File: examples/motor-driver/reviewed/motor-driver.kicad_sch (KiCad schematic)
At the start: 12 parts, among them J1 VM 2.7-10.8V, J2 MOTOR A, J3 MOTOR B, J4 LOGIC, U1 DRV8833PW

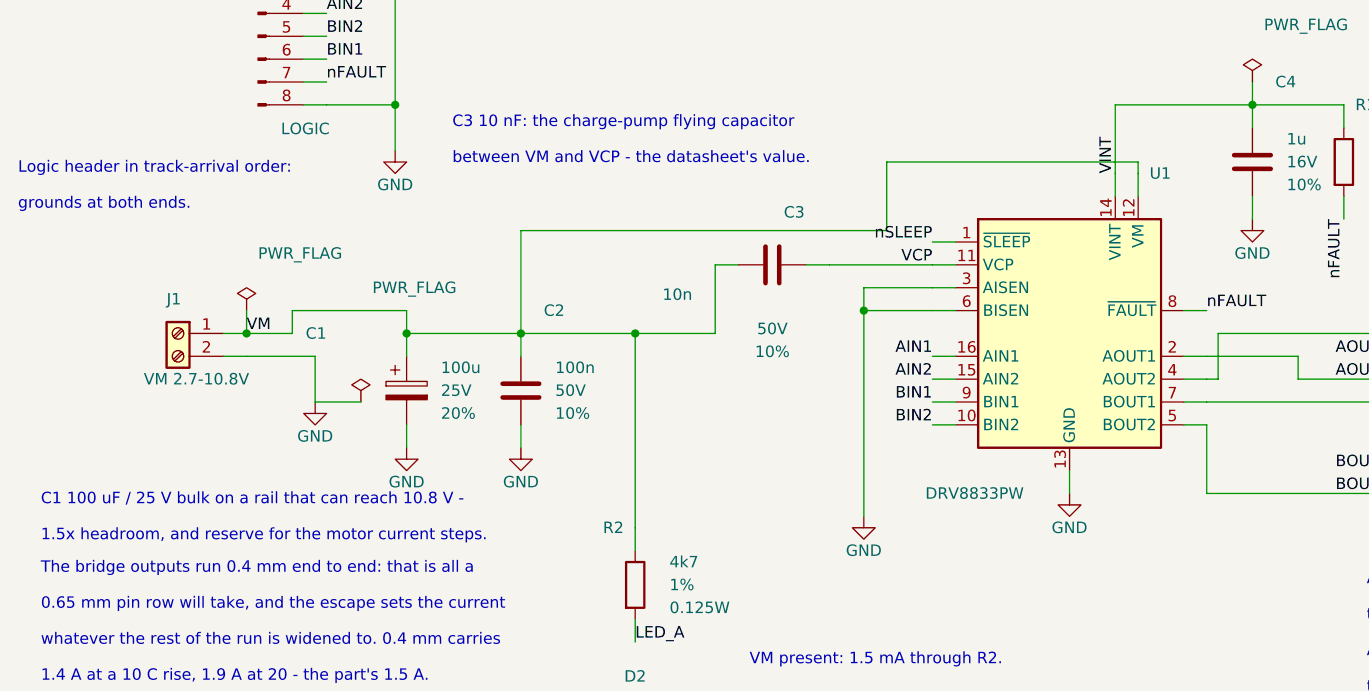
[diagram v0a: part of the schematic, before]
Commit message: Treat the ground plane as part of the drawing
Six reviewer circles, five of them the plane seen from different corners.
The pour now stops 1.2 mm inside the outline so an edge-hugging trace
keeps shell copper outside it; dead-end tongues narrower than 0.9 mm
retract instead of tapering to an acid-trap point in a bent corner; every
piece of the front pour over 8 mm2 holds a stitching via of its own,
placed before the orphan drop so a fenced-off strip gets a via instead of
staying a blank; and zone clearance comes down from 0.4 to 0.25, which is
what lets the plane flow between a 2.54 mm header's pins instead of
slotting the board top to bottom.

The round-twelve tee learns one manner: within two millimetres of the
goal it stands aside, so a rail flows through a bypass capacitor's pad
instead of feeding it by a stub - the carrier's bulk capacitor also moves
onto the VSYS run it was a millimetre south of. And
readability.margin_intrusion now measures symbol fields, power symbols
included: zero findings across KiCad's 18 demo sheets, one real catch on
our own motor sheet, whose power connector - like the FPGA board's -
moves in from the sheet edge so its printed name clears the frame.

Co-Authored-By: Claude Fable 5 <noreply@anthropic.com>
Claude-Session: https://claude.ai/code/session_01DUj7Ltu92tWg159mCSacwY
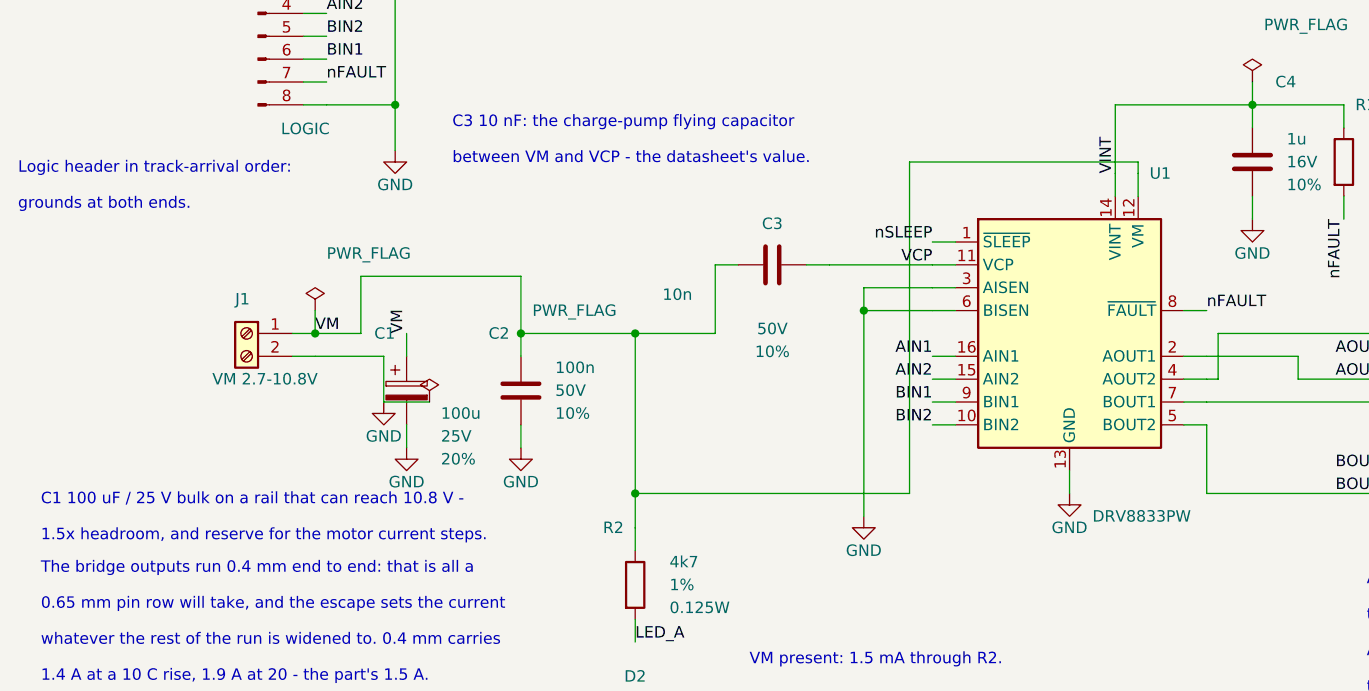
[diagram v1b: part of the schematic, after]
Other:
- moved on the sheet: J1

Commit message: Relieve the pads, fillet the joints, and give the board its screw holes
Three of the reviewer's manufacturing points, and they largely fall out
of the one before it - once KiCad fills the plane, the thermal relief it
was already asked for in the file actually appears.

**Thermal relief.** The zones said thermal all along; our own filler
ignored it and flooded every land solid. KiCad's does not, so every
through-hole ground pad now sits in a gap bridged by four spokes and an
iron can bring the joint up without heating a hundred square millimetres
of copper. `layout.solid_pad_connection` reports the setting when a
board turns it off: drilled pads only, because a surface pad reflows in
an oven that is heating the plane anyway and flooding it is often the
better thermal answer.

**Teardrops.** A track entering a land is a step change in width, and a
step change is where copper tears - the connector gets levered on and
off, the drill wanders, and the crack starts at the corner. `_teardrops`
replaces the first stretch of each run with a three-step taper into the
land, checked against its neighbours before it is kept, so a fillet
never eats the clearance a fine-pitch escape needs. It *replaces* rather
than overlays: laying the taper on top of the run drew the same copper
twice, and `route.acute_angle` reported all thirty of them, correctly.
`route.mixed_track_widths` learns what a fillet looks like so a properly
filleted board does not read as one nobody decided the width of.

**Mounting holes.** Four M3 holes near the corners, placed before the
router runs because they are obstacles, and slid along the edges or a
little inboard where a connector body has the corner - the motor board
and the op-amp take three, which is what those floorplans have room for.
Grounded on the motor driver, whose chassis is metal and part of the
shield, plain on the rest: bonding the enclosure to the reference is the
enclosure's decision, not the board's.

Two things that fell out of placing par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
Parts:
- added H1, H2, H3: M33, MountingHole:MountingHole_3.2mm_M3_Pad, symbol Mechanical:MountingHole_Pad
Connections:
- net GND: now also H1.1, H2.1, H3.1
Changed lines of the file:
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@@
     (instances (project "motor-driver" (path "/bddeec65-fa67-5f6a-9af2-d98e98d56e38" (reference "J4") (unit 1))))
+  )
+  (wire (pts (xy 25.4 172.72) (xy 25.4 175.26)) (stroke (width 0) (type default)))
+  (symbol (lib_id "Mechanical:MountingHole_Pad") (at 25.4 170.18 0.0) (unit 1)
+    (exclude_from_sim no) (in_bom yes) (on_board yes) (dnp no)
+    (property "Reference" "H1" (at 24.13 165.1 0) (effects (font (size 1.27 1.27)) (justify right)))
+    (property "Value" "M33" (at 29.21 173.99 0) (effects (font (size 1.27 1.27)) (justify left)))
+    (property "Footprint" "MountingHole:MountingHole_3.2mm_M3_Pad" (at 25.4 170.18 0) (effects (font (size 1.27 1.27)) hide))
+    (property "Datasheet" "~" (at 25.4 170.18 0) (effects (font (size 1.27 1.27)) hide))
+    (property "MPN" "n/a" (at 25.4 170.18 0) (effects (font (size 1.27 1.27)) hide))
+    (property "Manufacturer" "n/a" (at 25.4 170.18 0) (effects (font (size 1.27 1.27)) hide))
+    (pin "1" (uuid "6f7c7165-92db-566b-92dd-6318372b1c62-p1"))
+    (instances (project "motor-driver" (path "/bddeec65-fa67-5f6a-9af2-d98e98d56e38" (reference "H1") (unit 1))))
+  )
+  (wire (pts (xy 38.1 172.72) (xy 38.1 175.26)) (stroke (width 0) (type default)))
+  (symbol (lib_id "Mechanical:MountingHole_Pad") (at 38.099999999999994 170.18 0.0) (unit 1)
+    (exclude_from_sim no) (in_bom yes) (on_board yes) (dnp no)
+    (property "Reference" "H2" (at 36.83 165.1 0) (effects (font (size 1.27 1.27)) (justify right)))
+    (property "Value" "M33" (at 41.91 173.99 0) (effects (font (size 1.27 1.27)) (justify left)))
+    (property "Footprint" "MountingHole:MountingHole_3.2mm_M3_Pad" (at 38.099999999999994 170.18 0) (effects (font (size 1.27 1.27)) hide))
+    (property "Datasheet" "~" (at 38.099999999999994 170.18 0) (effects (font (size 1.27 1.27)) hide))
+    (property "MPN" "n/a" (at 38.099999999999994 170.18 0) (effects (font (size 1.27 1.27)) hide))
+    (property "Manufacturer" "n/a" (at 38.099999999999994 170.18 0) (effects (font (size 1.27 1.27)) hide))
+    (pin "1" (uuid "85bfd828-5616-57a0-9a28-764913f2f29c-p1"))
+    (instances (project "motor-driver" (path "/bddeec65-fa67-5f6a-9af2-d98e98d56e38" (reference "H2") (unit 1))))
+  )
+  (wire (pts (xy 50.8 172.72) (xy 50.8 175.26)) (stroke (width 0) (type default)))
+  (symbol (lib_id "Mechanical:MountingHole_Pad") (at 50.8 170.18 0.0) (unit 1)
+    (exclude_from_sim no) (in_bom yes) (on_board yes) (dnp no)
+    (property "Reference" "H3" (at 49.53 165.1 0) (effects (font (size 1.27 1.27)) (justify right)))
+    (property "Value" "M33" (at 54.61 173.99 0) (effects (font (size 1.27 1.27)) (justify left)))
+    (property "Footprint" "MountingHole:MountingHole_3.2mm_M3_Pad" (at 50.8 170.18 0) (effects (font (size 1.27 1.27)) hide))
+    (property "Datasheet" "~" (at 50.8 170.18 0) (effects (font (size 1.27 1.27)) hide))
+    (property "MPN" "n/a" (at 50.8 170.18 0) (effects (font (size 1.27 1.27)) hide))
+    (property "Manufacturer" "n/a" (at 50.8 170.18 0) (effects (font (size 1.27 1.27)) hide))
+    (pin "1" (uuid "b09ff8b6-9110-54ce-9289-a4d5206e7444-p1"))
+    (instances (project "motor-driver" (path "/bddeec65-fa67-5f6a-9af2-d98e98d56e38" (reference "H3") (unit 1))))
   )
   (wire (pts (xy 45.72 80.01) (xy 45.72 77.47)) (stroke (width 0) (type default)))
@@
     (instances (project "motor-driver" (path "/bddeec65-fa67-5f6a-9af2-d98e98d56e38" (reference "#PWR08") (unit 1))))
   )
+  (symbol (lib_id "power:GND") (at 25.4 175.26 0) (unit 1)
+    (exclude_from_sim no) (in_bom no) (on_board yes) (dnp no)
+    (property "Reference" "#PWR09" (at 25.4 175.26 0) (effects (font (size 1.27 1.27)) hide))
+    (property "Value" "GND" (at 25.4 179.07 0) (effects (font (size 1.27 1.27))))
+    (property "Footprint" "" (at 25.4 175.26 0) (effects (font (size 1.27 1.27)) hide))
+    (property "Datasheet" "" (at 25.4 175.26 0) (effects (font (size 1.27 1.27)) hide))
+    (pin "1" (uuid "23bbef0a-f984-5595-8bb3-a960ff1801cf-p"))
+    (instances (project "motor-driver" (path "/bddeec65-fa67-5f6a-9af2-d98e98d56e38" (reference "#PWR09") (unit 1))))
+  )
+  (symbol (lib_id "power:GND") (at 38.1 175.26 0) (unit 1)
+    (exclude_from_sim no) (in_bom no) (on_board yes) (dnp no)
+    (property "Reference" "#PWR10" (at 38.1 175.26 0) (effects (font (size 1.27 1.27)) hide))
+    (property "Value" "GND" (at 38.1 179.07 0) (effects (font (size 1.27 1.27))))
+    (property "Footprint" "" (at 38.1 175.26 0) (effects (font (size 1.27 1.27)) hide))
+    (property "Datasheet" "" (at 38.1 175.26 0) (effects (font (size 1.27 1.27)) hide))
+    (pin "1" (uuid "2265827e-ee6a-5b59-9134-c12204d3d65d-p"))
+    (instances (project "motor-driver" (path "/bddeec65-fa67-5f6a-9af2-d98e98d56e38" (reference "#PWR10") (unit 1))))
+  )
+  (symbol (lib_id "power:GND") (at 50.8 175.26 0) (unit 1)
+    (exclude_from_sim no) (in_bom no) (on_board yes) (dnp no)
+    (property "Reference" "#PWR11" (at 50.8 175.26 0) (effects (font (size 1.27 1.27)) hide))
+    (property "Value" "GND" (at 50.8 179.07 0) (effects (font (size 1.27 1.27))))
+    (property "Footprint" "" (at 50.8 175.26 0) (effects (font (size 1.27 1.27)) hide))
+    (property "Datasheet" "" (at 50.8 175.26 0) (effects (font (size 1.27 1.27)) hide))
+    (pin "1" (uuid "36f47f82-b430-5f2e-8c28-879d8277211b-p"))
+    (instances (project "motor-driver" (path "/bddeec65-fa67-5f6a-9af2-d98e98d56e38" (reference "#PWR11") (unit 1))))
+  )
   (symbol (lib_id "power:PWR_FLAG") (at 45.72 77.47 0) (unit 1)

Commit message: Give the assembly machine something to aim at
Fiducials: three copper dots in bare mask windows, near three different
corners so a pick-and-place gets rotation as well as offset. It aligns
to the board, not to the drawing - without them it has only the routed
outline, cut to a tolerance ten times looser than the placement a 0.5 mm
pitch part is asking for. `fab.no_fiducials` reports a fine-pitch board
that has none, as context rather than as a fault: plenty of boards are
built one at a time with tweezers.

They share the corner search with the mounting holes, which is where
this found a real bug: `_courtyard_box` read lines and rectangles only,
and a mounting hole draws its courtyard as one circle - so every hole
measured as taking up no room at all, and the first three fiducials
landed on top of three screw holes. Circles and arcs count now.

Co-Authored-By: Claude Fable 5 <noreply@anthropic.com>
Claude-Session: https://claude.ai/code/session_01DUj7Ltu92tWg159mCSacwY
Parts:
- added FID1, FID2, FID3: Fiducial, Fiducial:Fiducial_1mm_Mask2mm, symbol Mechanical:Fiducial
- H1, H2, H3: value M33 -> M3
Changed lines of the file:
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@@
     (exclude_from_sim no) (in_bom yes) (on_board yes) (dnp no)
     (property "Reference" "H1" (at 24.13 165.1 0) (effects (font (size 1.27 1.27)) (justify right)))
-    (property "Value" "M33" (at 29.21 173.99 0) (effects (font (size 1.27 1.27)) (justify left)))
+    (property "Value" "M3" (at 29.21 173.99 0) (effects (font (size 1.27 1.27)) (justify left)))
     (property "Footprint" "MountingHole:MountingHole_3.2mm_M3_Pad" (at 25.4 170.18 0) (effects (font (size 1.27 1.27)) hide))
     (property "Datasheet" "~" (at 25.4 170.18 0) (effects (font (size 1.27 1.27)) hide))
@@
     (exclude_from_sim no) (in_bom yes) (on_board yes) (dnp no)
     (property "Reference" "H2" (at 36.83 165.1 0) (effects (font (size 1.27 1.27)) (justify right)))
-    (property "Value" "M33" (at 41.91 173.99 0) (effects (font (size 1.27 1.27)) (justify left)))
+    (property "Value" "M3" (at 41.91 173.99 0) (effects (font (size 1.27 1.27)) (justify left)))
     (property "Footprint" "MountingHole:MountingHole_3.2mm_M3_Pad" (at 38.099999999999994 170.18 0) (effects (font (size 1.27 1.27)) hide))
     (property "Datasheet" "~" (at 38.099999999999994 170.18 0) (effects (font (size 1.27 1.27)) hide))
@@
     (exclude_from_sim no) (in_bom yes) (on_board yes) (dnp no)
     (property "Reference" "H3" (at 49.53 165.1 0) (effects (font (size 1.27 1.27)) (justify right)))
-    (property "Value" "M33" (at 54.61 173.99 0) (effects (font (size 1.27 1.27)) (justify left)))
+    (property "Value" "M3" (at 54.61 173.99 0) (effects (font (size 1.27 1.27)) (justify left)))
     (property "Footprint" "MountingHole:MountingHole_3.2mm_M3_Pad" (at 50.8 170.18 0) (effects (font (size 1.27 1.27)) hide))
     (property "Datasheet" "~" (at 50.8 170.18 0) (effects (font (size 1.27 1.27)) hide))
@@
     (instances (project "motor-driver" (path "/bddeec65-fa67-5f6a-9af2-d98e98d56e38" (reference "H3") (unit 1))))
   )
+  (symbol (lib_id "Mechanical:Fiducial") (at 63.5 170.18 0.0) (unit 1)
+    (exclude_from_sim no) (in_bom yes) (on_board yes) (dnp no)
+    (property "Reference" "FID1" (at 62.23 166.37 0) (effects (font (size 1.27 1.27)) (justify right)))
+    (property "Value" "Fiducial" (at 67.31 172.72 0) (effects (font (size 1.27 1.27)) (justify left)))
+    (property "Footprint" "Fiducial:Fiducial_1mm_Mask2mm" (at 63.5 170.18 0) (effects (font (size 1.27 1.27)) hide))
+    (property "Datasheet" "~" (at 63.5 170.18 0) (effects (font (size 1.27 1.27)) hide))
+    (property "MPN" "n/a" (at 63.5 170.18 0) (effects (font (size 1.27 1.27)) hide))
+    (property "Manufacturer" "n/a" (at 63.5 170.18 0) (effects (font (size 1.27 1.27)) hide))
+    (instances (project "motor-driver" (path "/bddeec65-fa67-5f6a-9af2-d98e98d56e38" (reference "FID1") (unit 1))))
+  )
+  (symbol (lib_id "Mechanical:Fiducial") (at 76.2 170.18 0.0) (unit 1)
+    (exclude_from_sim no) (in_bom yes) (on_board yes) (dnp no)
+    (property "Reference" "FID2" (at 74.93 166.37 0) (effects (font (size 1.27 1.27)) (justify right)))
+    (property "Value" "Fiducial" (at 80.01 172.72 0) (effects (font (size 1.27 1.27)) (justify left)))
+    (property "Footprint" "Fiducial:Fiducial_1mm_Mask2mm" (at 76.2 170.18 0) (effects (font (size 1.27 1.27)) hide))
+    (property "Datasheet" "~" (at 76.2 170.18 0) (effects (font (size 1.27 1.27)) hide))
+    (property "MPN" "n/a" (at 76.2 170.18 0) (effects (font (size 1.27 1.27)) hide))
+    (property "Manufacturer" "n/a" (at 76.2 170.18 0) (effects (font (size 1.27 1.27)) hide))
+    (instances (project "motor-driver" (path "/bddeec65-fa67-5f6a-9af2-d98e98d56e38" (reference "FID2") (unit 1))))
+  )
+  (symbol (lib_id "Mechanical:Fiducial") (at 88.9 170.18 0.0) (unit 1)
+    (exclude_from_sim no) (in_bom yes) (on_board yes) (dnp no)
+    (property "Reference" "FID3" (at 87.63 166.37 0) (effects (font (size 1.27 1.27)) (justify right)))
+    (property "Value" "Fiducial" (at 92.71 172.72 0) (effects (font (size 1.27 1.27)) (justify left)))
+    (property "Footprint" "Fiducial:Fiducial_1mm_Mask2mm" (at 88.9 170.18 0) (effects (font (size 1.27 1.27)) hide))
+    (property "Datasheet" "~" (at 88.9 170.18 0) (effects (font (size 1.27 1.27)) hide))
+    (property "MPN" "n/a" (at 88.9 170.18 0) (effects (font (size 1.27 1.27)) hide))
+    (property "Manufacturer" "n/a" (at 88.9 170.18 0) (effects (font (size 1.27 1.27)) hide))
+    (instances (project "motor-driver" (path "/bddeec65-fa67-5f6a-9af2-d98e98d56e38" (reference "FID3") (unit 1))))
+  )
   (wire (pts (xy 45.72 80.01) (xy 45.72 77.47)) (stroke (width 0) (type default)))

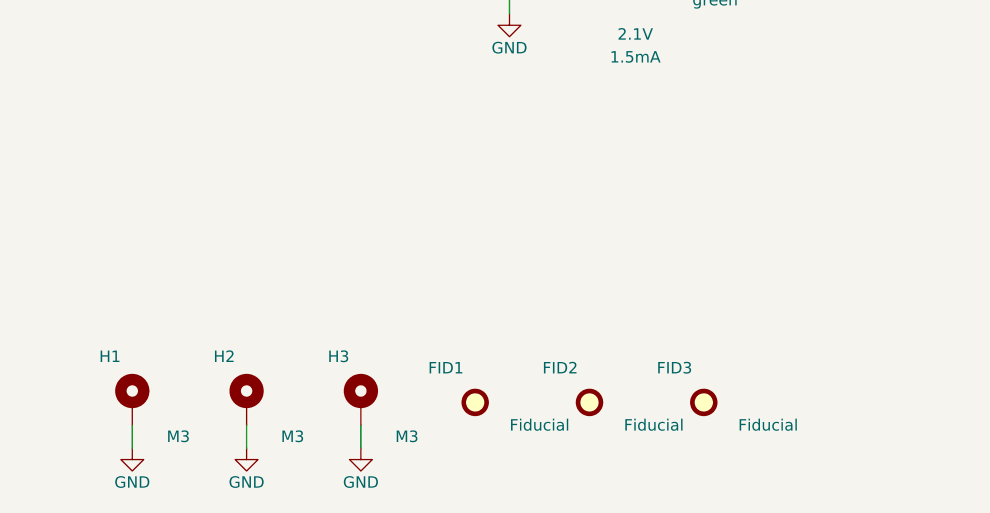
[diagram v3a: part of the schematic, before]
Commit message: Let the new parts sit somewhere sensible, on the board and on the sheet
Placing screw holes and fiducials turned up four things that were wrong
before either existed, all of them about where something is allowed to
go rather than about the parts themselves.

A designator was kept off the pads but not inside the board outline, so
any part at the edge - a connector, and now a hole - had its reference
clipped by the edge. Every board had been carrying one or two of those.

A symbol with no pins leaves no trace in the sheet planner's obstacle
list, because that list is built from pin stubs. The screw holes were
invisible to it and the fiducials landed on top of them. The free-row
search also ran off the right-hand edge of an A4 page and sat over the
title block on the way, which is `readability.outside_page` and
`readability.margin_intrusion` respectively - both real, both now
avoided by bounding the search to the drawing area.

And the bill-of-materials flag is read from the footprint rather than
the symbol library, because the footprint is the side KiCad's parity
check reads and the side the fab agrees with. That retired three
warnings the op-amp board had been carrying since it gained test
points: `Connector:TestPoint` claims to be a BOM line and its own
footprint says otherwise.

All four fast boards pass their gates; the suite is green on 10.0.4.

Co-Authored-By: Claude Fable 5 <noreply@anthropic.com>
Claude-Session: https://claude.ai/code/session_01DUj7Ltu92tWg159mCSacwY
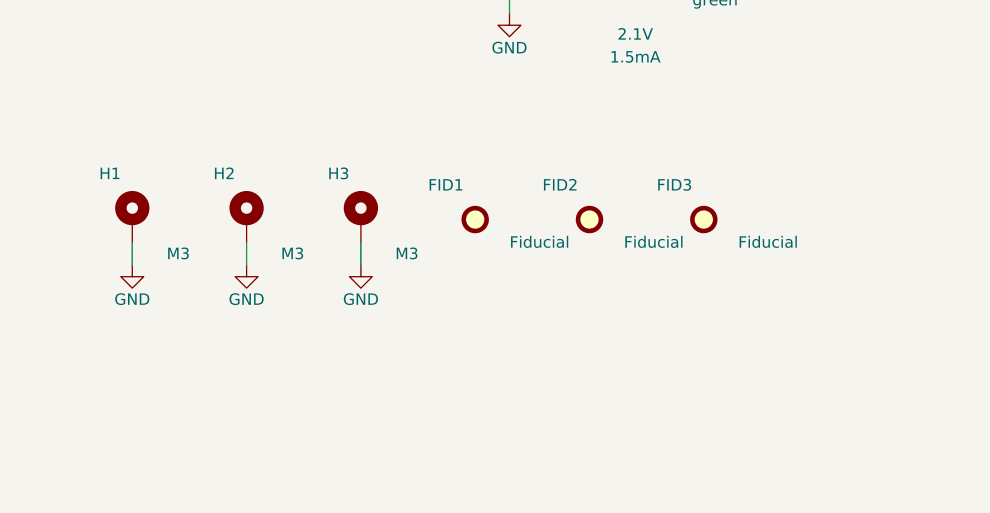
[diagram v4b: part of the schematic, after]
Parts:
- FID1, FID2, FID3, H1, H2, H3: now left out of the parts list
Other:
- moved on the sheet: FID1, FID2, FID3, H1, H2, H3
